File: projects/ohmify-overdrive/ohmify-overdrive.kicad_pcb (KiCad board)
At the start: 2 copper layers, 44.2 x 40.1 mm, 18 parts, among them J1 InputJack, J2 OutputJack, U1 LM358

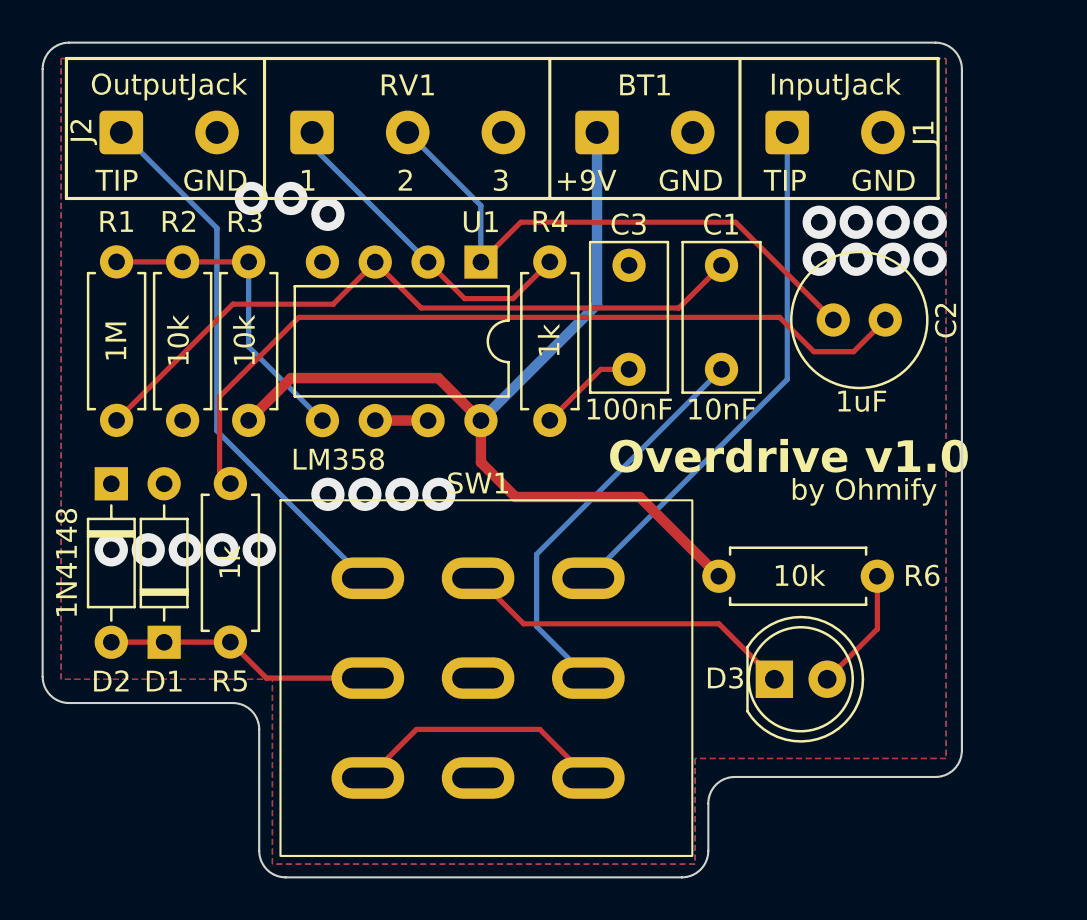
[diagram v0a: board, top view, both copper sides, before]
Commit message: Fixed 3DPT symbol for the overdrive
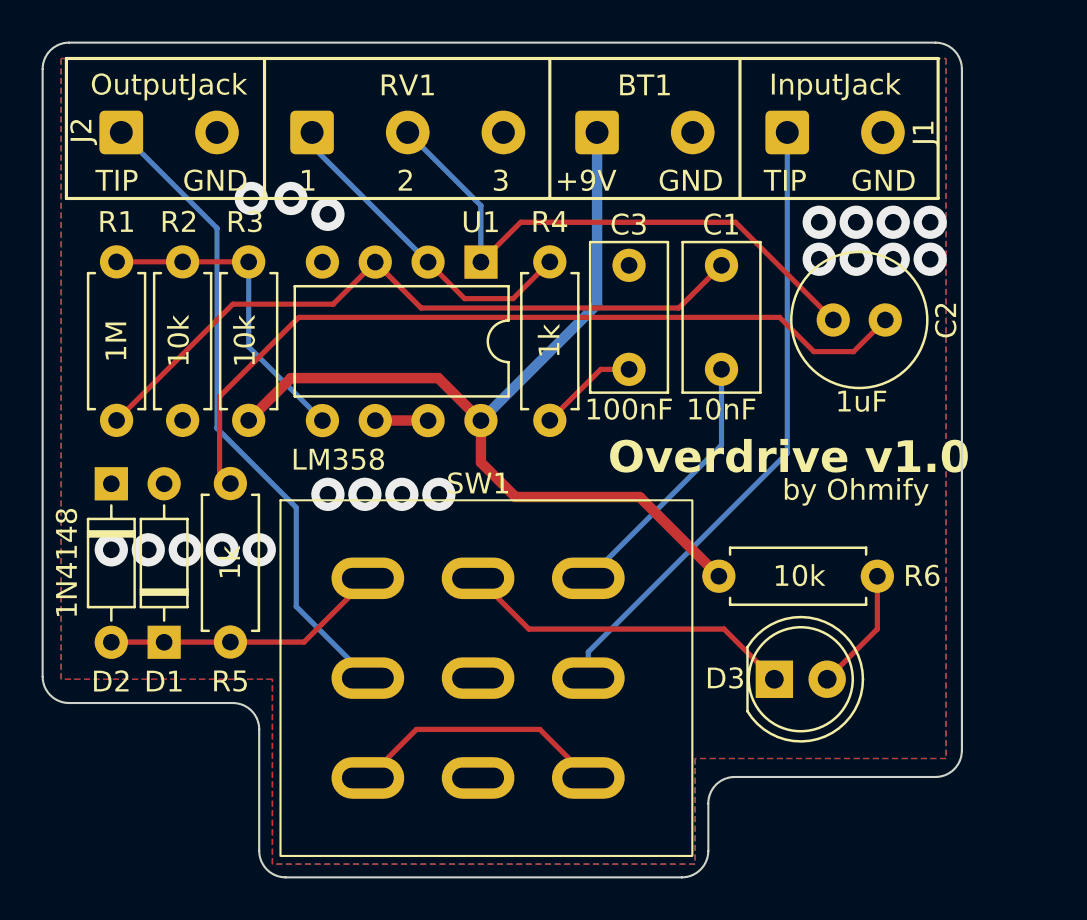
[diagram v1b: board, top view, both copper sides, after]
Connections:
- SW1 pad 1: Net-(J2-PadT) -> OUTPUT
- SW1 pad 2: OUTPUT -> Net-(J2-PadT)
- SW1 pad 7: Net-(J1-PadT) -> INPUT
- SW1 pad 8: INPUT -> Net-(J1-PadT)
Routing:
- net INPUT: track 19.6 -> 12.7 mm
- net Net-(J1-PadT): track 25.4 -> 30.2 mm
- net Net-(J2-PadT): track 26.4 -> 31.1 mm
- net OUTPUT: track 13.1 -> 13.8 mm

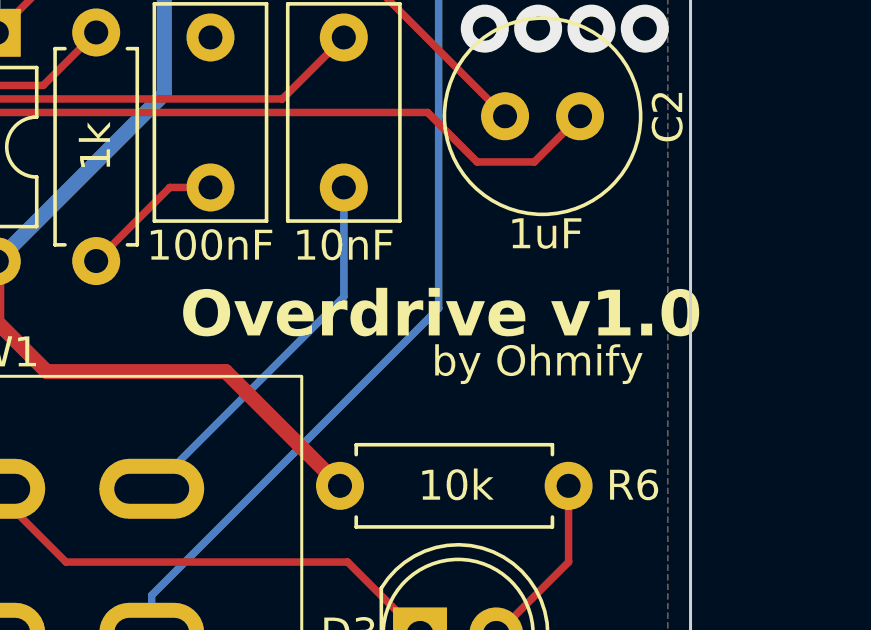
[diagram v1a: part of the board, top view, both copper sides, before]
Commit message: Fixed synthcard, added new gerber files
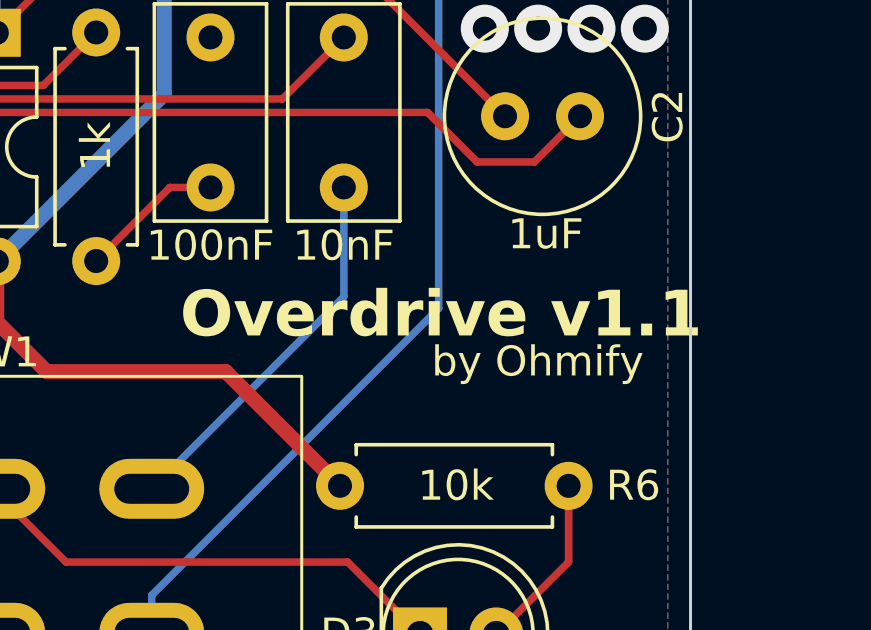
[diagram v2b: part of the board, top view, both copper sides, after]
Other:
- board text added: "Overdrive v1.1"
- board text removed: "Overdrive v1.0"
